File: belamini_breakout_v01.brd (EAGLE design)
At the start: 61 x 128.5 mm, 5 parts, among them J1 M10SILK_FEMALE_PTH

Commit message: schematic components and layout
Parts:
- added A0J, A1J, A2J, A3J, A4J, A5J, A6J, A7J, ADC1, ADC2, ALOL, ALOR, DAC1, DAC2: WQP-PJ301M-12_JACK, thonkiconn:WQP-PJ301M-12_JACK
- added C1, C12, C15, C17, C19, C21, C23, C26, C3, C5, C7, C9: 1n, resistor:C0603
- added C10, C11, C13, C18, C2, C20, C22, C24, C25, C27, C28, C4, C6, C8: 10u, resistor:C0603
- added C14, C16: 100u, resistor:C0603
- added C29, C30, C31, C32, C33, C34: (no value), resistor:C0603
- added C35, C51: 100n, rcl:C0603
- added C52, C53: 47u, rcl:PANASONIC_D
- added D1, D2, D3, D4: WHITE, SparkFun-LED:LED-1206
- added D10, D9: 1N5819HW, diode:SOD123
- added IC1, IC3, IC5: TL074D, linear:SO14
- added IC10: LM4040B10, texas:DBZ_R-PDSO-G3
- added IC2: LM4041CIDBZ, texas:DBZ_R-PDSO-G3
- added J3, J4: (no value), SparkFun-Connectors:1X03
- added JP2: M05X2PTH, og-header:AVR_ICSP
- added R1, R13, R18, R20, R24, R26, R33, R37, R41, R45, R5, R9: 3k3, resistor:R0603
- added R10, R14, R19, R2, R22, R27, R28, R29, R30, R31, R32, R34, R38, R42, R46, R49, R50, R51, R56, R57, R6: 10k, resistor:R0603
- added R11, R12, R15, R16, R17, R21, R3, R35, R36, R39, R4, R40, R43, R44, R47, R48, R7, R8: 100k, resistor:R0603
- added R23, R25: 33k, resistor:R0603
- added R52, R53, R54, R55: 470, resistor:R0603
- added R58, R62: 470, rcl:R0603
- added S1, S2, S3, S4, S5, S6, S7, S8: MOMENTARY-SWITCH-SPST-SMD-6.2MM-TALL, SparkFun-Switches:TACTILE_SWITCH_SMD_6.2MM_TALL
- added SW1: EC12E_SW, switch-alps:ALPS_EC12E_SW
- added VR1, VR10, VR11, VR12, VR2, VR3, VR4, VR9: 10k, SparkFun-Resistors:POT-PTH-ALPS-KIT
- U$1: value WQP-PJ301M-12_JACK -> RECOM785.0; device thonkiconn:WQP-PJ301M-12_JACK -> audioic:R-78XX-1.0
- moved U$1 36.5 mm to (63.2, 85.9), flipped to the top, turned to 270 degrees
- moved J2 35.1 mm to (27.3, 44.6), flipped to the bottom
- moved P2 31.7 mm to (41.3, 48.5), flipped to the bottom
- moved P1 31.7 mm to (41.3, 23.1), flipped to the bottom
- moved J1 31.0 mm to (40.1, 44.7), flipped to the bottom
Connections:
- removed net 3V3: P1.14, P2.23
- new net +12V: C30.1, C31.1, C34.1, C52.+, D9.C, IC1.4, IC3.4, IC5.4, U$1.VIN
- new net +3V3: P1.14, P2.23, R27.2, R30.2, R31.2, R32.2, R49.2, R50.2, R51.2, R56.2, R57.2
- new net -10V: C51.1, IC10.2, R62.2, VR1.P$1, VR10.P$1, VR11.P$1, VR12.P$1, VR2.P$1, VR3.P$1, VR4.P$1, VR9.P$1
- new net -12V: C29.2, C32.2, C33.2, C53.-, D10.A, IC1.11, IC3.11, IC5.11, R62.1
- new net 1V2: C35.1, IC1.10, IC1.12, IC1.3, IC1.5, IC2.2, IC3.3, IC3.5, IC5.10, IC5.12, IC5.3, IC5.5, R58.2
- new net ADC1: C11.2, C12.2, IC3.7, J3.3, R19.2
- new net ADC2: C10.2, C9.2, IC3.1, J3.2, R22.2
- new net DAC1: J4.3, R24.1
- new net DAC2: J4.2, R26.1
- new net N$1: A0J.P$1, R3.1
- new net N$10: R11.2, R12.2, R9.1
- new net N$11: A1J.P$1, R11.1
- new net N$12: R12.1, VR3.P$2
- new net N$13: C7.1, IC1.6, R13.2, R14.1
- new net N$14: R13.1, R15.2, R16.2
- new net N$15: A3J.P$1, R15.1
- new net N$16: R16.1, VR4.P$2
- new net N$17: C21.1, IC5.9, R41.2, R42.1
- new net N$18: C19.1, IC5.6, R37.2, R38.1
- new net N$19: C23.1, IC5.13, R45.2, R46.1
- new net N$2: C1.1, IC1.9, R1.2, R2.1
- new net N$20: ADC1.P$1, R17.1
- new net N$21: R17.2, R18.1
- new net N$22: C12.1, IC3.6, R18.2, R19.1
- new net N$23: C9.1, IC3.2, R20.2, R22.1
- new net N$24: C26.1, IC3.9, R25.1, R26.2
- new net N$25: R20.1, R21.2
- new net N$26: ADC2.P$1, R21.1
- new net N$27: C14.2, DAC1.P$1
- new net N$28: C13.1, C14.1, C15.2, IC3.14, R23.2
- new net N$29: C15.1, IC3.13, R23.1, R24.2
- new net N$3: R1.1, R3.2, R4.2
- new net N$30: D4.A, R55.1
- new net N$31: C16.1, C25.1, C26.2, IC3.8, R25.2
- new net N$32: C16.2, DAC2.P$1
- new net N$33: C17.1, IC5.2, R33.2, R34.1
- new net N$34: R33.1, R35.2, R36.2
- new net N$35: A4J.P$1, R35.1
- new net N$36: R36.1, VR9.P$2
- new net N$37: D3.A, R54.1
- new net N$38: R37.1, R39.2, R40.2
- new net N$39: A5J.P$1, R39.1
- new net N$4: R4.1, VR1.P$2
- new net N$40: R40.1, VR10.P$2
- new net N$41: D2.A, R53.1
- new net N$42: R41.1, R43.2, R44.2
- new net N$43: A6J.P$1, R43.1
- new net N$44: R44.1, VR11.P$2
- new net N$45: D1.A, R52.1
- new net N$46: R45.1, R47.2, R48.2
- new net N$47: A7J.P$1, R47.1
- new net N$48: R48.1, VR12.P$2
- new net N$5: C3.1, IC1.2, R5.2, R6.1
- new net N$52: D9.A, JP2.1, JP2.2
- new net N$53: D10.C, JP2.10, JP2.9
- new net N$6: R5.1, R7.2, R8.2
- new net N$7: A2J.P$1, R7.1
- new net N$8: R8.1, VR2.P$2
- new net N$9: C5.1, IC1.13, R10.1, R9.2
- new net SCL: P2.9
- new net SDA: P2.11
- net 5V: now also R58.1, U$1.VOUT
- net A0: now also C1.2, C2.2, IC1.8, R2.2
- net A1: now also C5.2, C6.2, IC1.14, R10.2
- net A2: now also C3.2, C4.2, IC1.1, R6.2
- net A3: now also C7.2, C8.2, IC1.7, R14.2
- net A4: now also C17.2, C18.2, IC5.1, R34.2
- net A5: now also C19.2, C20.2, IC5.7, R38.2
- net A6: now also C21.2, C22.2, IC5.8, R42.2
- net A7: now also C23.2, C24.2, IC5.14, R46.2
- net D0: now also R55.2
- net D1: now also R54.2
- net D10: now also R30.1, S1.A2
- net D11: now also R49.1, S4.A2
- net D13: now also R27.1, SW1.E
- net D14: now also C28.2, R29.2, SW1.A
- net D15: now also C27.1, R28.1, SW1.B
- net D2: now also R53.2
- net D3: now also R52.2
- net D4: now also R57.1, S8.A2
- net D5: now also R56.1, S7.A2
- net D6: now also R50.1, S5.A2
- net D7: now also R51.1, S6.A2
- net D8: now also R32.1, S3.A2
- net D9: now also R31.1, S2.A2
- net GND: now also A0J.P$2, A0J.P$3, A1J.P$2, A1J.P$3, A2J.P$2, A2J.P$3, A3J.P$2, A3J.P$3, A4J.P$2, A4J.P$3, A5J.P$2, A5J.P$3, A6J.P$2, A6J.P$3, A7J.P$2, A7J.P$3, ADC1.P$2, ADC1.P$3, ADC2.P$2, ADC2.P$3, C10.1, C11.1, C13.2, C18.1, C2.1, C20.1, C22.1, C24.1, C25.2, C27.2, C28.1, C29.1, C30.2, C31.2, C32.1, C33.1, C34.2, C35.2, C4.1, C51.2, C52.-, C53.+, C6.1, C8.1, D1.C, D2.C, D3.C, D4.C, DAC1.P$3, DAC2.P$2, DAC2.P$3, IC10.1, IC2.3, IC3.10, IC3.12, J3.1, J4.1, JP2.3, JP2.4, JP2.5, JP2.6, JP2.7, JP2.8, R28.2, R29.1, S1.B2, S2.B2, S3.B2, S4.B2, S5.B2, S6.B2, S7.B2, S8.B2, SW1.C, SW1.D, U$1.GND, VR1.P$3, VR10.P$3, VR11.P$3, VR12.P$3, VR2.P$3, VR3.P$3, VR4.P$3, VR9.P$3
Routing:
- net -10V: track 0.00 -> 116.3 mm
- net A3: track 0.00 -> 94.5 mm
- net A7: track 0.00 -> 90.7 mm, vias 0 -> 1
- net A1: track 0.00 -> 90.4 mm, vias 0 -> 1
- net A2: track 0.00 -> 89.5 mm, vias 0 -> 1
- net A0: track 0.00 -> 88.8 mm, vias 0 -> 1
- net A4: track 0.00 -> 85.5 mm
- net A5: track 0.00 -> 83.1 mm, vias 0 -> 1
- net A6: track 0.00 -> 82.9 mm, vias 0 -> 1
- net N$4: track 0.00 -> 67.1 mm, vias 0 -> 1
- net +12V: track 0.00 -> 53.3 mm, vias 0 -> 1
- net N$44: track 0.00 -> 53.0 mm
- net N$48: track 0.00 -> 49.1 mm
- net 1V2: track 0.00 -> 45.1 mm, vias 0 -> 3
- net N$40: track 0.00 -> 42.4 mm
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- added copper zone on layer 3, net +12V
- added copper zone on layer 3, net -12V
- added copper zone on layer 3, net 5V
- added copper zone on layer 2, net GND
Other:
- board size 61 x 128.5 mm -> 71.1 x 128.5 mm
- board text removed: "SW1"

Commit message: minimise features and layout
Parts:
- removed A4J, A5J, A6J, A7J: WQP-PJ301M-12_JACK, thonkiconn:WQP-PJ301M-12_JACK
- removed C17, C19, C21, C23: 1n, resistor:C0603
- removed C18, C20, C22, C24: 10u, resistor:C0603
- removed C29, C30: (no value), resistor:C0603
- removed IC5: TL074D, linear:SO14
- removed R33, R37, R41, R45: 3k3, resistor:R0603
- removed R34, R38, R42, R46: 10k, resistor:R0603
- removed R35, R36, R39, R40, R43, R44, R47, R48: 100k, resistor:R0603
- removed VR10, VR11, VR12, VR9: 10k, SparkFun-Resistors:POT-PTH-ALPS-KIT
- moved C51 98.4 mm to (22.8, 95.2)
- moved R62 97.8 mm to (20.6, 95.2)
- moved IC10 93.6 mm to (17.5, 95.7), turned to 0 degrees
- moved C31 81.2 mm to (16.9, 82.5), turned to 90 degrees
- moved C32 70.5 mm to (27.3, 81.7), turned to 270 degrees
- moved R15 68.7 mm to (1.90, 56.2), turned to 270 degrees
- moved VR4 67.7 mm to (6.47, 47.4), flipped to the bottom, turned to 180 degrees
- moved R16 66.8 mm to (4.00, 54.5), turned to 90 degrees
- moved R13 63.2 mm to (6.10, 56.2), turned to 90 degrees
- moved R17 61.8 mm to (1.50, 1.80), turned to 90 degrees
- moved ADC1 61.8 mm to (4.60, 6.25)
- moved R18 60.7 mm to (2.30, 13.3)
- moved R14 60.4 mm to (8.20, 56.2), turned to 270 degrees
- moved A3J 59.8 mm to (7.08, 61.1), turned to 270 degrees
- moved C7 57.6 mm to (10.3, 56.2), turned to 270 degrees
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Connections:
- removed net 1V2: C35.1, IC1.10, IC1.12, IC1.3, IC1.5, IC2.2, IC3.3, IC3.5, IC5.10, IC5.12, IC5.3, IC5.5, R58.2
- removed net 5V: P1.24, R58.1, U$1.VOUT
- removed net N$17: C21.1, IC5.9, R41.2, R42.1
- removed net N$18: C19.1, IC5.6, R37.2, R38.1
- removed net N$19: C23.1, IC5.13, R45.2, R46.1
- removed net N$33: C17.1, IC5.2, R33.2, R34.1
- removed net N$34: R33.1, R35.2, R36.2
- removed net N$35: A4J.P$1, R35.1
- removed net N$36: R36.1, VR9.P$2
- removed net N$38: R37.1, R39.2, R40.2
- removed net N$39: A5J.P$1, R39.1
- removed net N$40: R40.1, VR10.P$2
- removed net N$42: R41.1, R43.2, R44.2
- removed net N$43: A6J.P$1, R43.1
- removed net N$44: R44.1, VR11.P$2
- removed net N$46: R45.1, R47.2, R48.2
- removed net N$47: A7J.P$1, R47.1
- removed net N$48: R48.1, VR12.P$2
- new net +5V: P1.24, U$1.VOUT
- new net VCC: C35.1, IC1.10, IC1.12, IC1.3, IC1.5, IC2.2, IC3.3, IC3.5, R58.2
- net +12V: no longer C30.1, IC5.4
- net +3V3: now also C27.2, C28.1, R58.1, SW1.C
- net -10V: no longer VR10.P$1, VR11.P$1, VR12.P$1, VR9.P$1
- net -12V: no longer C29.2, IC5.11
- net A0: now also IC1.14; no longer IC1.8
- net A1: now also IC1.1; no longer IC1.14
- net A2: now also IC1.7; no longer IC1.1
- net A3: now also IC1.8; no longer IC1.7
- net A4: no longer C17.2, C18.2, IC5.1, R34.2
- net A5: no longer C19.2, C20.2, IC5.7, R38.2
- net A6: no longer C21.2, C22.2, IC5.8, R42.2
- net A7: no longer C23.2, C24.2, IC5.14, R46.2
- net ADC1: now also IC3.1; no longer IC3.7
- net ADC2: now also IC3.7; no longer IC3.1
- net D10: now also R56.1, S7.A2; no longer R30.1, S1.A2
- net D11: now also R57.1, S8.A2; no longer R49.1, S4.A2
- net D4: now also R30.1, S1.A2; no longer R57.1, S8.A2
- net D5: now also R31.1, S2.A2; no longer R56.1, S7.A2
- net D6: now also R32.1, S3.A2; no longer R50.1, S5.A2
- net D7: now also R49.1, S4.A2; no longer R51.1, S6.A2
- net D8: now also R50.1, S5.A2; no longer R32.1, S3.A2
- net D9: now also R51.1, S6.A2; no longer R31.1, S2.A2
- net GND: no longer A4J.P$2, A4J.P$3, A5J.P$2, A5J.P$3, A6J.P$2, A6J.P$3, A7J.P$2, A7J.P$3, C18.1, C20.1, C22.1, C24.1, C27.2, C28.1, C29.1, C30.2, SW1.C, VR10.P$3, VR11.P$3, VR12.P$3, VR9.P$3
- net N$13: now also IC1.9; no longer IC1.6
- net N$2: now also IC1.13; no longer IC1.9
- net N$22: now also IC3.2; no longer IC3.6
- net N$23: now also IC3.6; no longer IC3.2
- net N$5: now also IC1.6; no longer IC1.2
- net N$9: now also IC1.2; no longer IC1.13
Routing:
- net +3V3: track 17.0 -> 152.5 mm, vias 0 -> 3
- net A7: track 90.7 -> 0.00 mm, vias 1 -> 0
- net A4: track 85.5 -> 0.00 mm
- net A5: track 83.1 -> 0.00 mm, vias 1 -> 0
- net A6: track 82.9 -> 0.00 mm, vias 1 -> 0
- net N$27: track 2.25 -> 58.6 mm
- net N$44: track 53.0 -> 0.00 mm
- net N$4: track 67.1 -> 16.3 mm, vias 1 -> 0
- net N$48: track 49.1 -> 0.00 mm
- net 1V2: track 45.1 -> 0.00 mm, vias 3 -> 0
- net A2: track 89.5 -> 44.7 mm, vias 1 -> 0
- net N$40: track 42.4 -> 0.00 mm
- net ADC1: track 23.2 -> 65.0 mm
- net D14: track 21.3 -> 62.8 mm
- net N$36: track 40.2 -> 0.00 mm
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- added copper zone on layer 16, net +12V
- added copper zone on layer 3, net +3V3
- added copper zone on layer 3, net +5V
- added copper zone on layer 16, net -12V
- added copper zone on layer 3, net VCC
- removed copper zone on layer 3, net 5V
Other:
- board size 71.1 x 128.5 mm -> 71.1 x 105 mm
- board text added: "+12V"
- board text added: "-12V"
- board text added: "3v3"

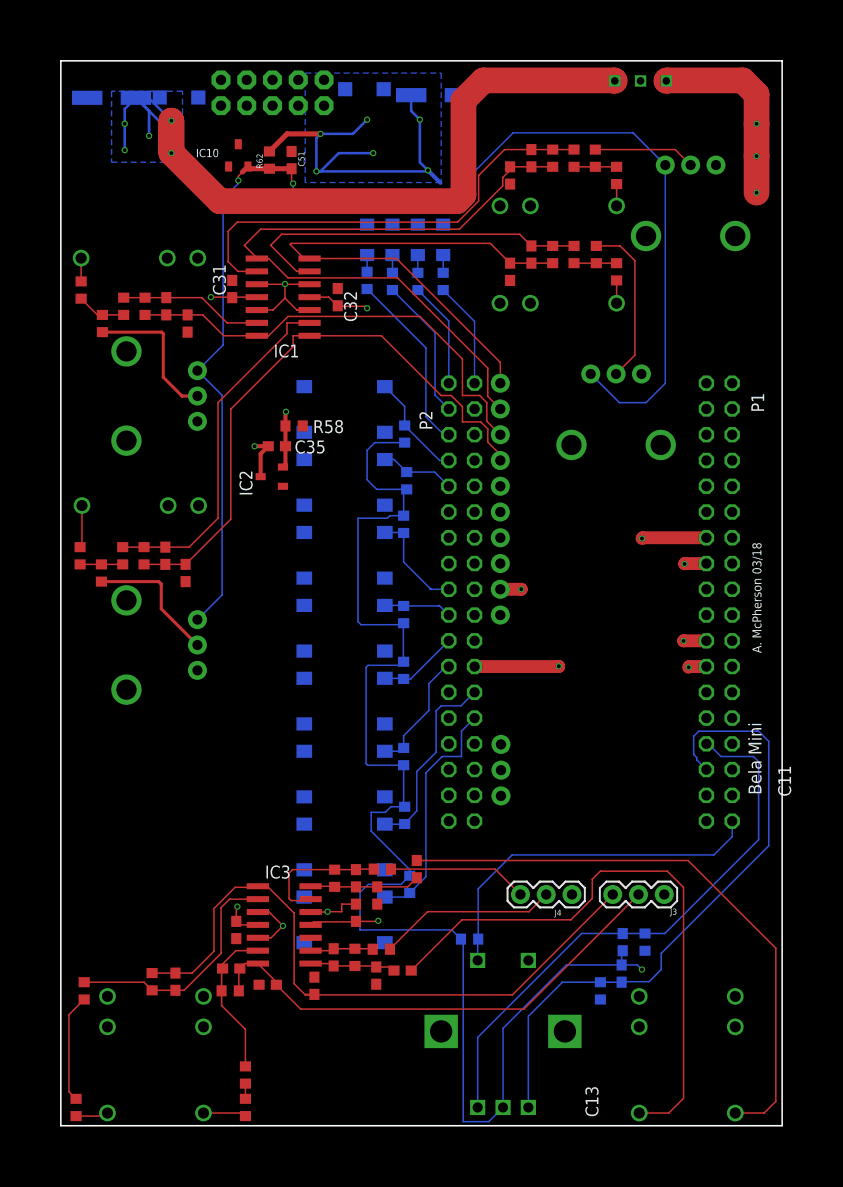
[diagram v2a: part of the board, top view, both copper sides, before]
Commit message: gorund plane front and back and make 4 layer
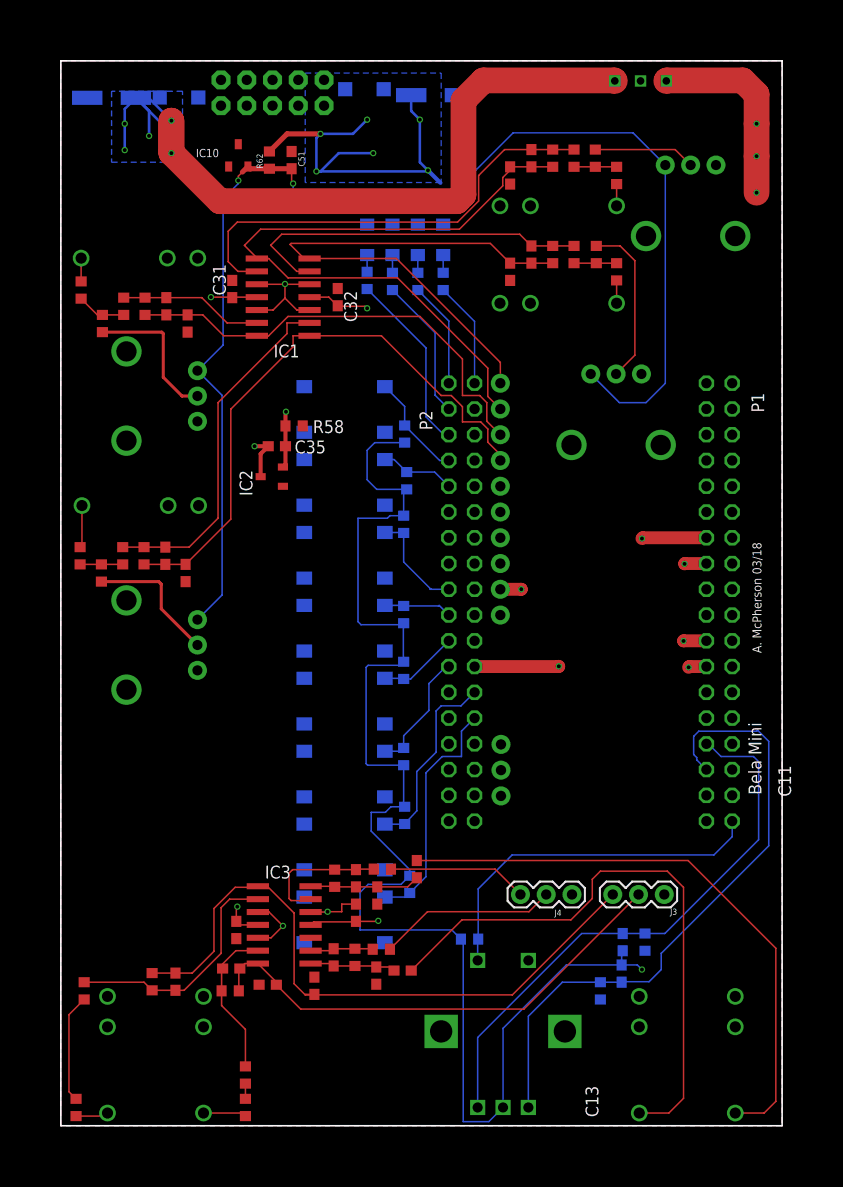
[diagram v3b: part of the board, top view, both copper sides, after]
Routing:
- added copper zone on layer 1, net GND
- added copper zone on layer 16, net GND
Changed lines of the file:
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@@
 <wire x1="24.625" y1="21.07" x2="26.27" y2="21.07" width="0.1524" layer="1"/>
 <wire x1="26.27" y1="21.07" x2="26.3" y2="21.1" width="0.1524" layer="1"/>
-<wire x1="44.3" y1="92.85" x2="39.345" y2="101.615" width="0" layer="19" extent="1-16"/>
-<wire x1="43.3" y1="90.7" x2="44.3" y2="92.85" width="0" layer="19" extent="1-1"/>
-<wire x1="31.2" y1="21.85" x2="29.1" y2="21.85" width="0" layer="19" extent="1-1"/>
-<wire x1="44.3" y1="83.35" x2="43.3" y2="81.1" width="0" layer="19" extent="1-1"/>
-<wire x1="24.625" y1="18.53" x2="24.625" y2="21.07" width="0" layer="19" extent="1-1"/>
-<wire x1="31.94966875" y1="25.23580625" x2="31.2" y2="21.85" width="0" layer="19" extent="1-16"/>
-<wire x1="53.2" y1="12.45" x2="57.0333375" y2="12.75" width="0" layer="19" extent="16-16"/>
-<wire x1="31.94966875" y1="18.046075" x2="31.2" y2="21.85" width="0" layer="19" extent="1-16"/>
-<wire x1="25" y1="14.65" x2="24.625" y2="18.53" width="0" layer="19" extent="1-1"/>
-<wire x1="16.9" y1="83.35" x2="13.5" y2="85.55" width="0" layer="19" extent="1-1"/>
-<wire x1="31.1" y1="13.95" x2="31.94966875" y2="18.046075" width="0" layer="19" extent="1-16"/>
-<wire x1="57.6" y1="17.25" x2="57.0333375" y2="12.75" width="0" layer="19" extent="16-16"/>
-<wire x1="22.755" y1="96.0625" x2="23.4125" y2="100.58" width="0" layer="19" extent="1-1"/>
-<wire x1="19.55" y1="13.9" x2="25" y2="14.65" width="0" layer="19" extent="1-1"/>
-<wire x1="17.3" y1="18.45" x2="19.55" y2="13.9" width="0" layer="19" extent="1-1"/>
-<wire x1="37.69999375" y1="88.85" x2="43.3" y2="90.7" width="0" layer="19" extent="16-16"/>
-<wire x1="35.19999375" y1="88.85" x2="37.69999375" y2="88.85" width="0" layer="19" extent="16-16"/>
-<wire x1="32.69999375" y1="88.85" x2="35.19999375" y2="88.85" width="0" layer="19" extent="16-16"/>
-<wire x1="30.19999375" y1="88.85" x2="32.69999375" y2="88.85" width="0" layer="19" extent="16-16"/>
-<wire x1="16.5475" y1="94.58" x2="18.3325" y2="100.58" width="0" layer="19" extent="1-1"/>
-<wire x1="12.5" y1="78.25" x2="16.9" y2="83.35" width="0" layer="19" extent="1-1"/>
+<polygon width="0.1524" layer="16">
+<vertex x="0" y="0"/>
+<vertex x="0" y="105"/>
+<vertex x="71.1" y="105"/>
+<vertex x="71.1" y="0"/>
+</polygon>
+<polygon width="0.1524" layer="1">
+<vertex x="0" y="0"/>
+<vertex x="0" y="105"/>
+<vertex x="71.1" y="105"/>
+<vertex x="71.1" y="0"/>
+</polygon>
 <wire x1="27.3" y1="82.55" x2="30.19999375" y2="88.85" width="0" layer="19" extent="1-16"/>
-<wire x1="31.94966875" y1="32.4255375" x2="31.94966875" y2="25.23580625" width="0" layer="19" extent="16-16"/>
-<wire x1="31.94966875" y1="39.61526875" x2="31.94966875" y2="32.4255375" width="0" layer="19" extent="16-16"/>
-<wire x1="31.94966875" y1="46.805" x2="31.94966875" y2="39.61526875" width="0" layer="19" extent="16-16"/>
-<wire x1="31.94966875" y1="53.99473125" x2="31.94966875" y2="46.805" width="0" layer="19" extent="16-16"/>
-<wire x1="31.94966875" y1="61.1844625" x2="31.94966875" y2="53.99473125" width="0" layer="19" extent="16-16"/>
-<wire x1="31.94966875" y1="68.37419375" x2="31.94966875" y2="61.1844625" width="0" layer="19" extent="16-16"/>
-<wire x1="12.3" y1="53.65" x2="13.5834" y2="61.15" width="0" layer="19" extent="1-1"/>
-<wire x1="2.6" y1="101.3575" x2="16.5475" y2="94.58" width="0" layer="19" extent="1-16"/>
 </signal>
 <signal name="REF">

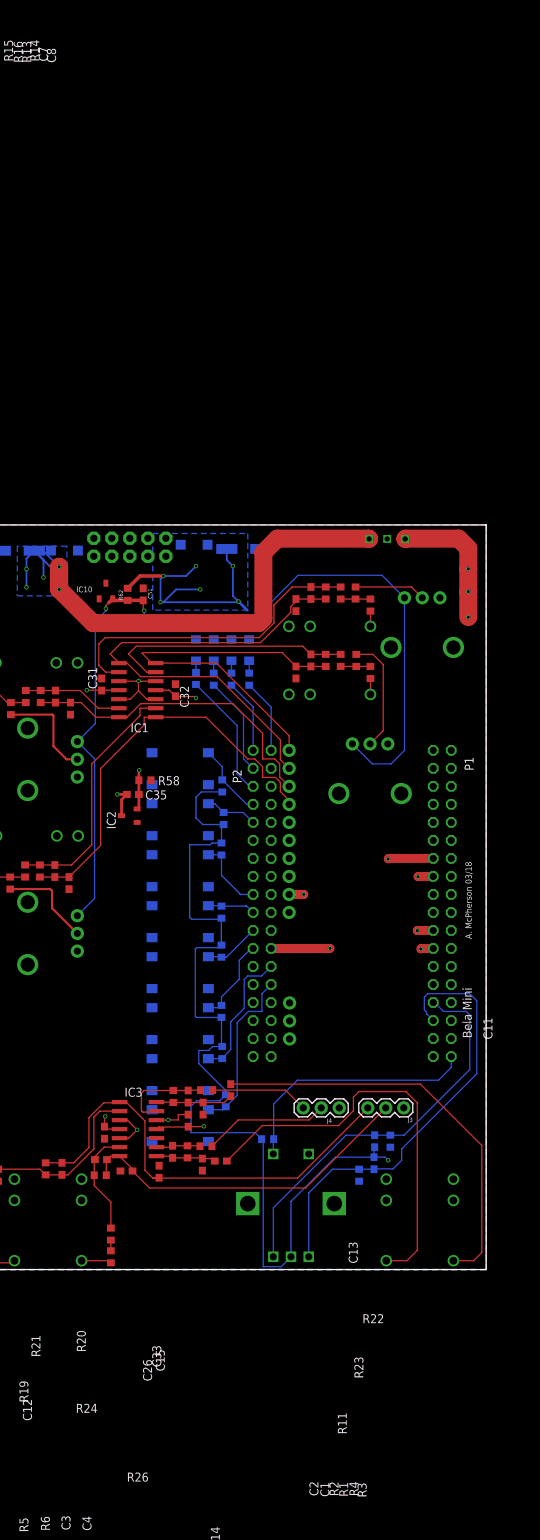
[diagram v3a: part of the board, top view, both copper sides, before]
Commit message: clear out all DRV (except priority)
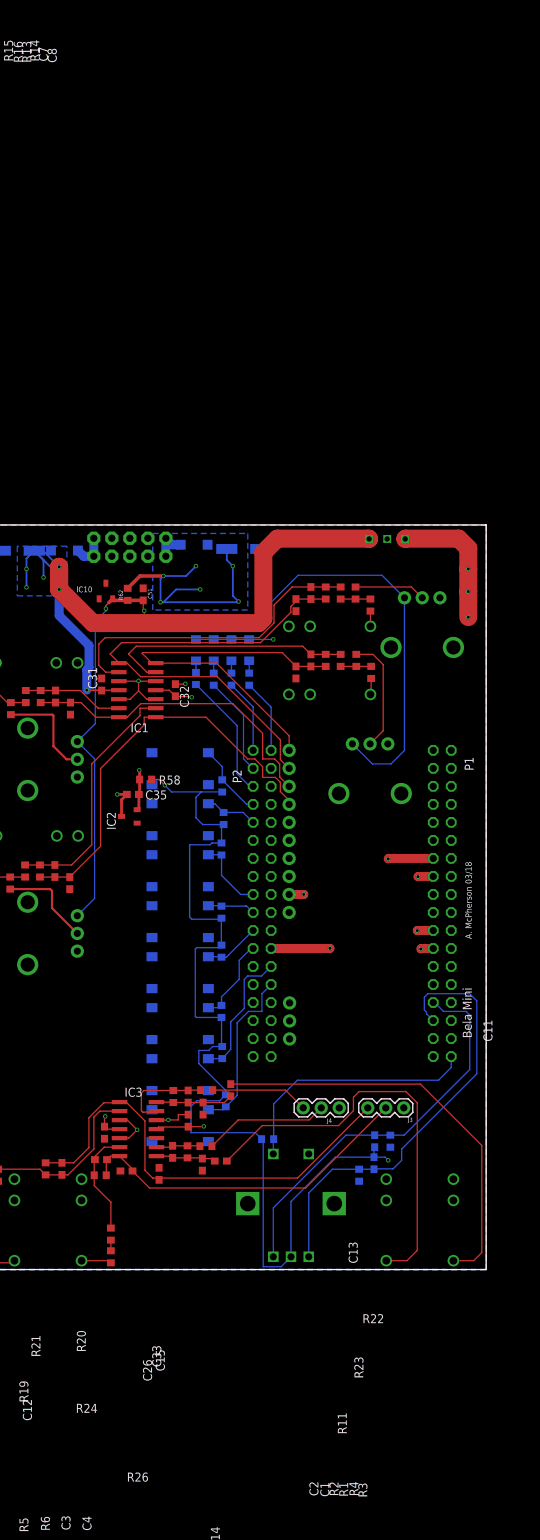
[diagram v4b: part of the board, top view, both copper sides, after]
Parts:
- moved C11 0.30 mm to (25.0, 13.5)
- moved R58 0.14 mm to (23.1, 69.1)
- moved IC2 0.10 mm to (20.8, 63.9)
- moved R3 0.10 mm to (54.9, 84.2)
- moved C8 0.10 mm to (12.4, 54.5)
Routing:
- net +12V: track 92.0 -> 110.2 mm
- net GND: track 16.4 -> 28.8 mm, vias 5 -> 7
- net +3V3: track 152.5 -> 160.3 mm, vias 3 -> 4
- net N$52: track 0.00 -> 5.11 mm
- net N$53: track 0.00 -> 5.00 mm
- net -12V: track 55.0 -> 52.7 mm
- net ADC1: track 65.0 -> 64.4 mm
